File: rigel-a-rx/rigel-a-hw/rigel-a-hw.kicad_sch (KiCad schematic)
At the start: 39 parts, among them IC1 BALFHB-WL-02D3, J1 Conn_01x03_Pin, J3 Conn_01x03_Pin, U1 STM32WLE5C8Ux, U2 XC6206P332MR, U3 CH340X, U4 TYPE-C_16PIN_2MD(073), U5 X1G004131004200, U6 KH-SMA-K513-G

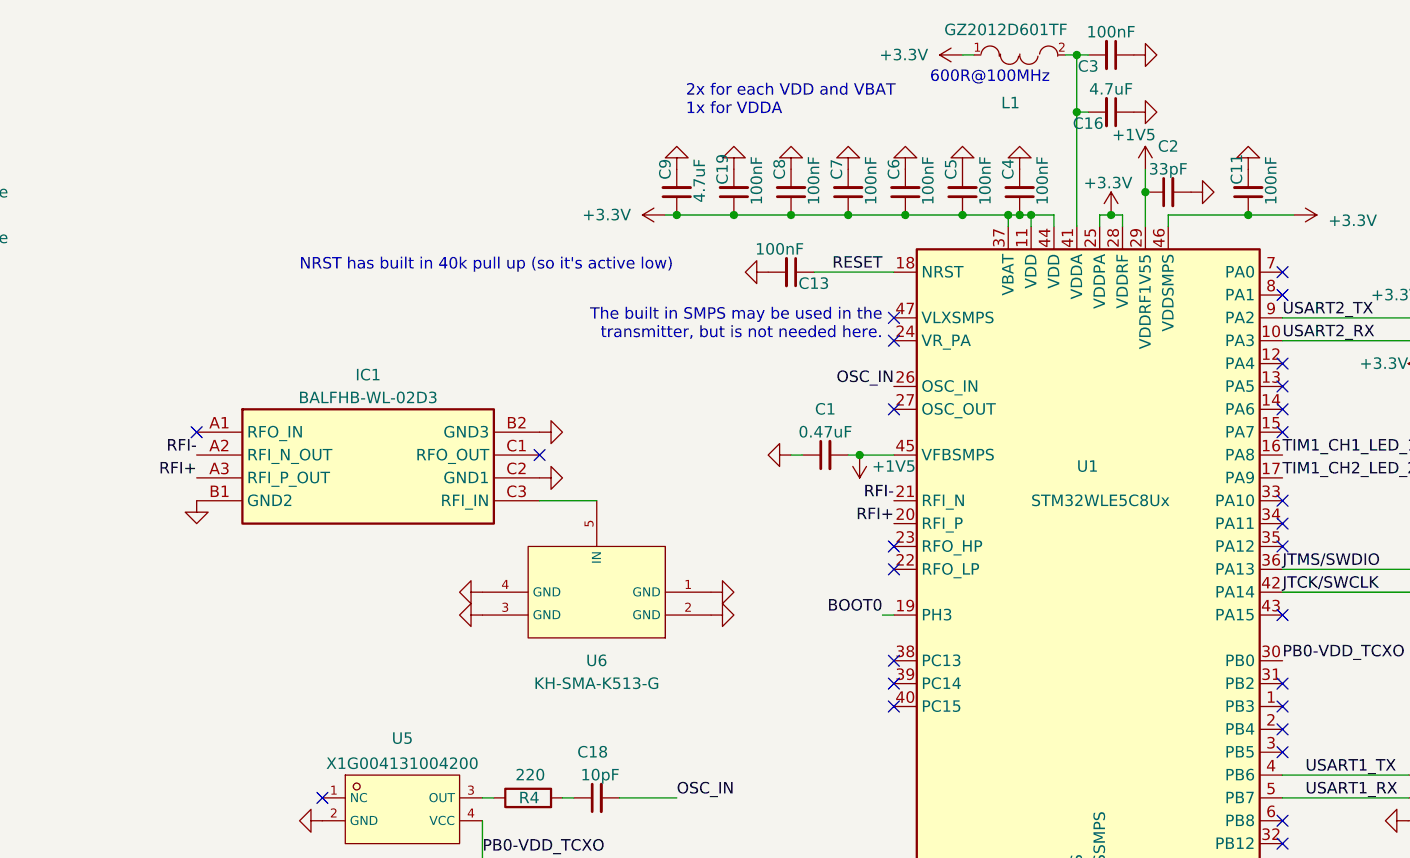
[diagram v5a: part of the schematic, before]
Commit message: basic RX test working
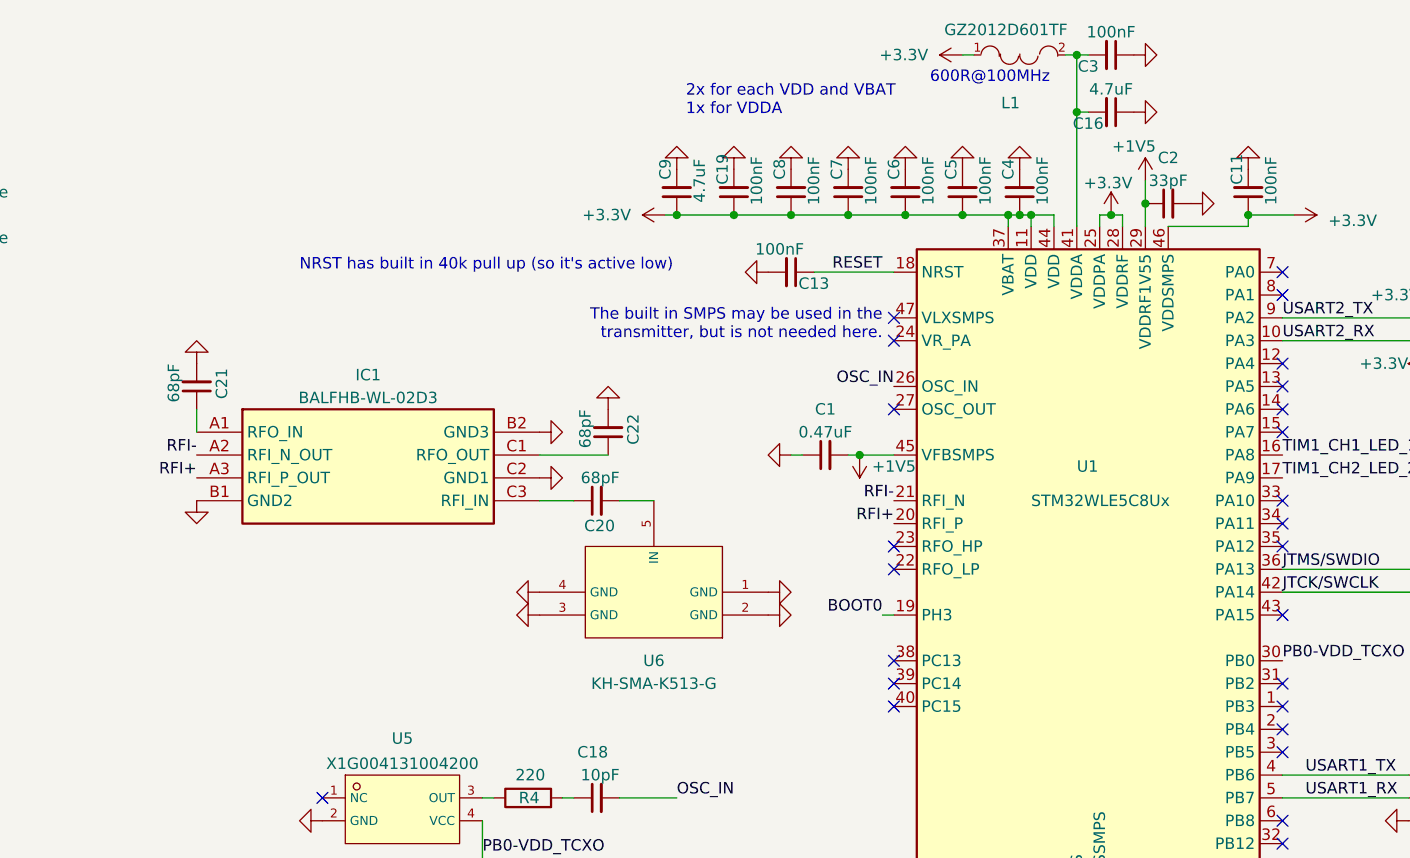
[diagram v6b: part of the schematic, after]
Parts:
- added C20, C21, C22: 68pF, Capacitor_SMD:C_0402_1005Metric, symbol Device:C_Small
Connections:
- net GND: now also C21.2, C22.2
- net at IC1.C3 (RFI_IN): now also C20.1; no longer U6.5 (IN)
- net at IC1.A1 (RFO_IN): now also C21.1
- net at IC1.C1 (RFO_OUT): now also C22.1
- new net: C20.2, U6.5 (IN)
- no-connect marks 32 -> 30
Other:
- moved on the sheet: C2, U6
